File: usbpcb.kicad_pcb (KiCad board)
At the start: 2 copper layers, 32.5 x 56 mm, 6 parts, among them J1 USB_A, J2 USB3_A, J3 Conn_02x05_Counter_Clockwise, J4 Conn_02x05_Counter_Clockwise

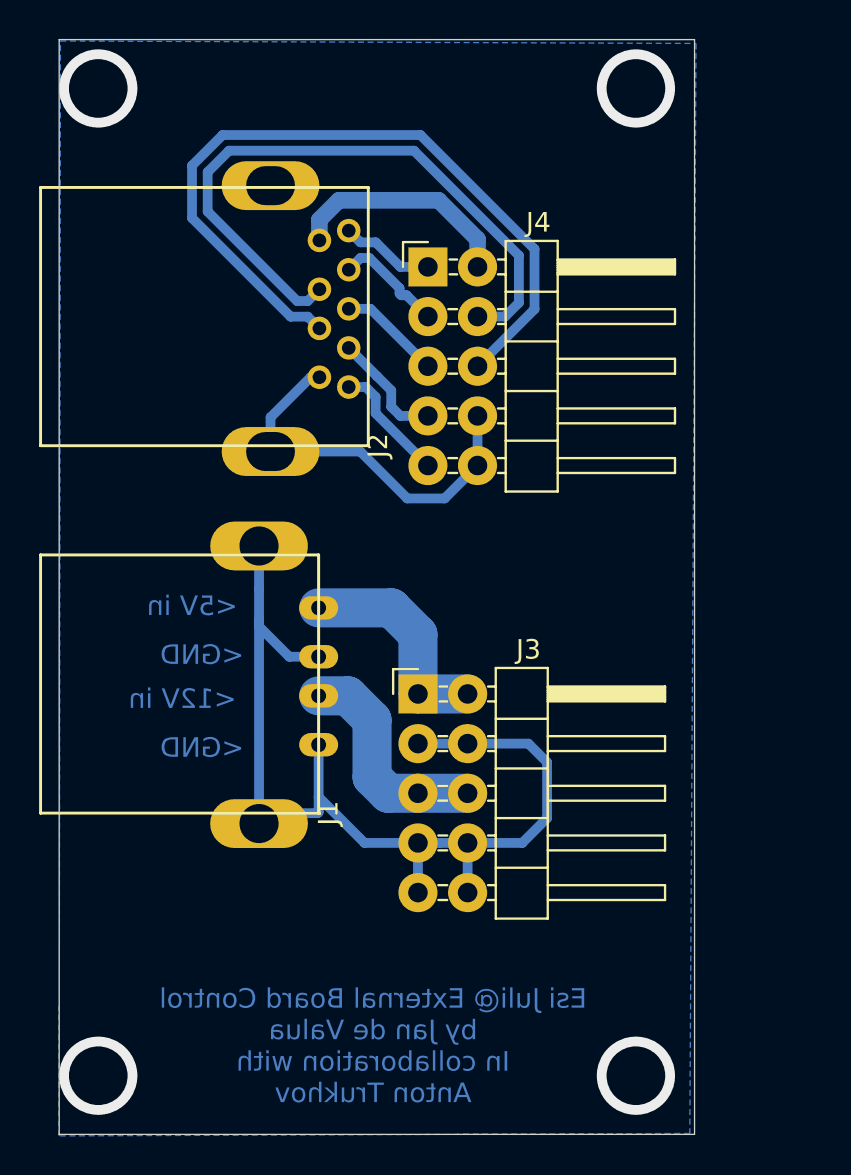
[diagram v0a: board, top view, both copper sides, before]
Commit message: Alternative variant of location and routing traces
Alternative variant of location and routing traces, because first try of connection was failed and it's still needs to be verified, what was the reason: bad cable. bad soldiering or PCB design errors, so if problem in PCB - this branch will be to next try.
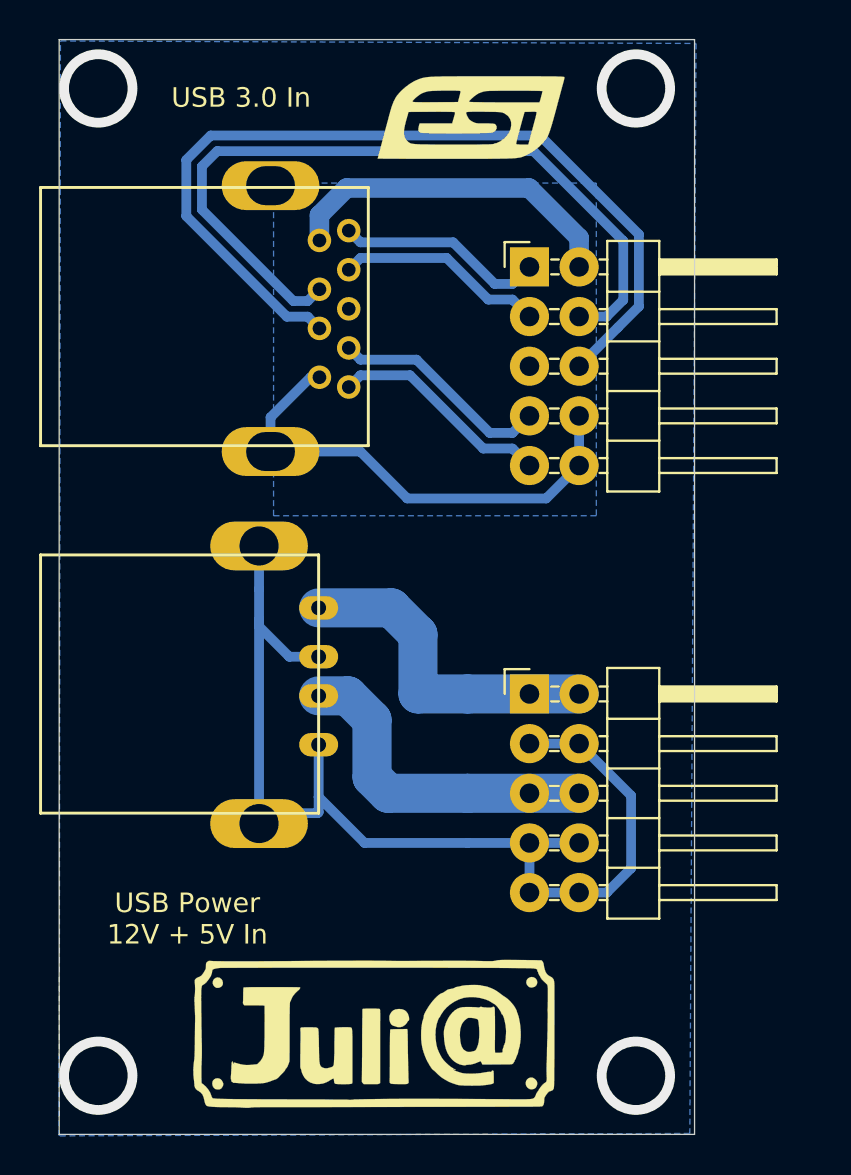
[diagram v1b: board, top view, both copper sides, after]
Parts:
- moved J3 5.70 mm to (55.0, 65.2)
- moved J4 5.20 mm to (55.0, 43.4)
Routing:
- net GND: track 72.6 -> 82.3 mm
- net /D_P: track 39.3 -> 45.8 mm
- net /D_N: track 33.3 -> 39.8 mm
- net /SR_N: track 4.82 -> 10.7 mm
- net Net-(J2-Pad1): track 11.8 -> 17.7 mm
- net /5V: track 11.2 -> 16.9 mm
- net /12V: track 11.4 -> 17.1 mm
- net /ST_N: track 5.98 -> 11.4 mm
- net Net-(J2-Pad7): track 5.26 -> 0.00 mm
- net /ST_P: track 6.23 -> 11.4 mm
- net /SR_P: track 5.70 -> 10.7 mm
- added copper zone on B.Cu, net Net-(J2-Pad7)

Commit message: update
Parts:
- moved J3 1.75 mm to (56.8, 65.2)
- moved J4 1.75 mm to (56.8, 43.4)
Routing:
- net GND: track 82.3 -> 5.91 mm
- net Net-(J2-Pad1): track 17.7 -> 20.2 mm
- net /D_N: track 39.8 -> 41.6 mm
- net /ST_P: track 11.4 -> 13.2 mm
- net /ST_N: track 11.4 -> 13.2 mm
- net /SR_N: track 10.7 -> 12.5 mm
- net /D_P: track 45.8 -> 47.6 mm
- net /5V: track 16.9 -> 18.7 mm
- net /SR_P: track 10.7 -> 12.5 mm
- net /12V: track 17.1 -> 18.9 mm
